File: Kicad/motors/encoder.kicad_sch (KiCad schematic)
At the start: 12 parts

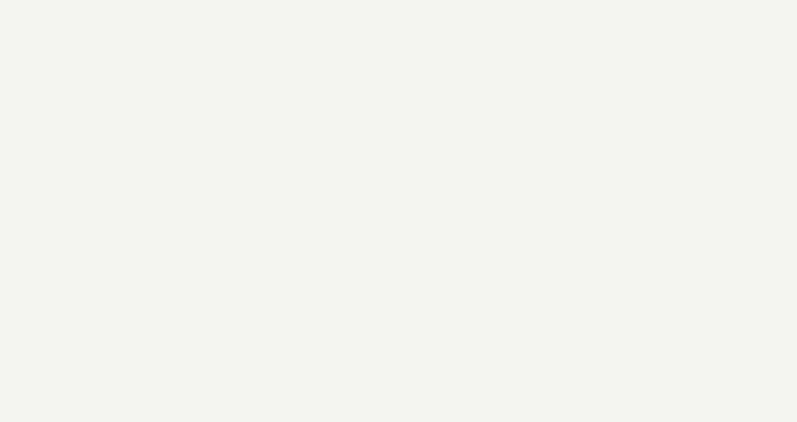
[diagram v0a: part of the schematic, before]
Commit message: Update Motors
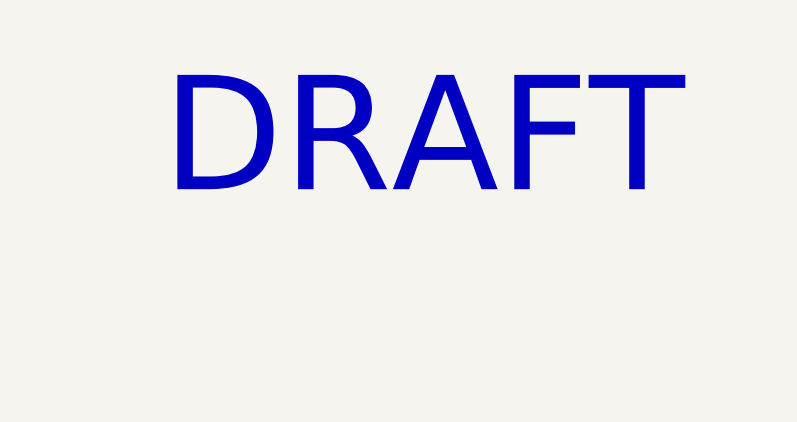
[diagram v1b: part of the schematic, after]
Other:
- note added: "DRAFT"
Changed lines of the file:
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@@
     (stroke (width 0) (type solid) (color 0 0 0 0))
+  )
+  (text "DRAFT" (at 127 93.98 0)
+    (effects (font (size 12.7 12.7)) (justify left bottom))
   )
   (symbol (lib_id "tronixio:SN74LVC1G19-SOT") (at 116.84 177.8 0) (unit 2)

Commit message: Update Motor
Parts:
- removed IC? (x4): SN74LVC1G19-SOT, tronixio:SOT-23-6, symbol tronixio:SN74LVC1G19-SOT
- removed TP?: KEYSTONE-5006, tronixio:KEYSTONE-5006, symbol tronixio:KEYSTONE-5006
- added C? (x2): 1µ, tronixio:CAPACITOR-1206, symbol tronixio:C-1206
- added R? (x2): 10K, tronixio:RESISTOR-1206, symbol tronixio:R-1206
- added TP?: HARWIN-S1751, tronixio:zzzHARWIN-S1751, symbol tronixio:HARWIN-S1751
- C? (x2): value C-1206 -> 100n; Name 100n -> (none)
- C? (x2): value C-1206 -> 1µ; Name 1µ -> (none)
- IC?: value LM3480-33-SOT -> LM3480-33; Name LM3480-33 -> (none)
- LED?: value LED-1206-ORANGE -> +3V3; symbol tronixio:LED-1206-ORANGE -> tronixio:LED-1206-RED; MOUSER 604-APT3216LSECKJ4RV -> 604-APT3216LSECKJ3RV
- R?: value R-1206 -> 6K8; Name 6K8 -> (none)
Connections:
- net +5V is gone; now on net +3V3: C?.1, C?.1, R?.1
- net +3V3: now also C?.1, C?.1, R?.1, R?.1, TP?.1
- net GND: now also C?.2, C?.2

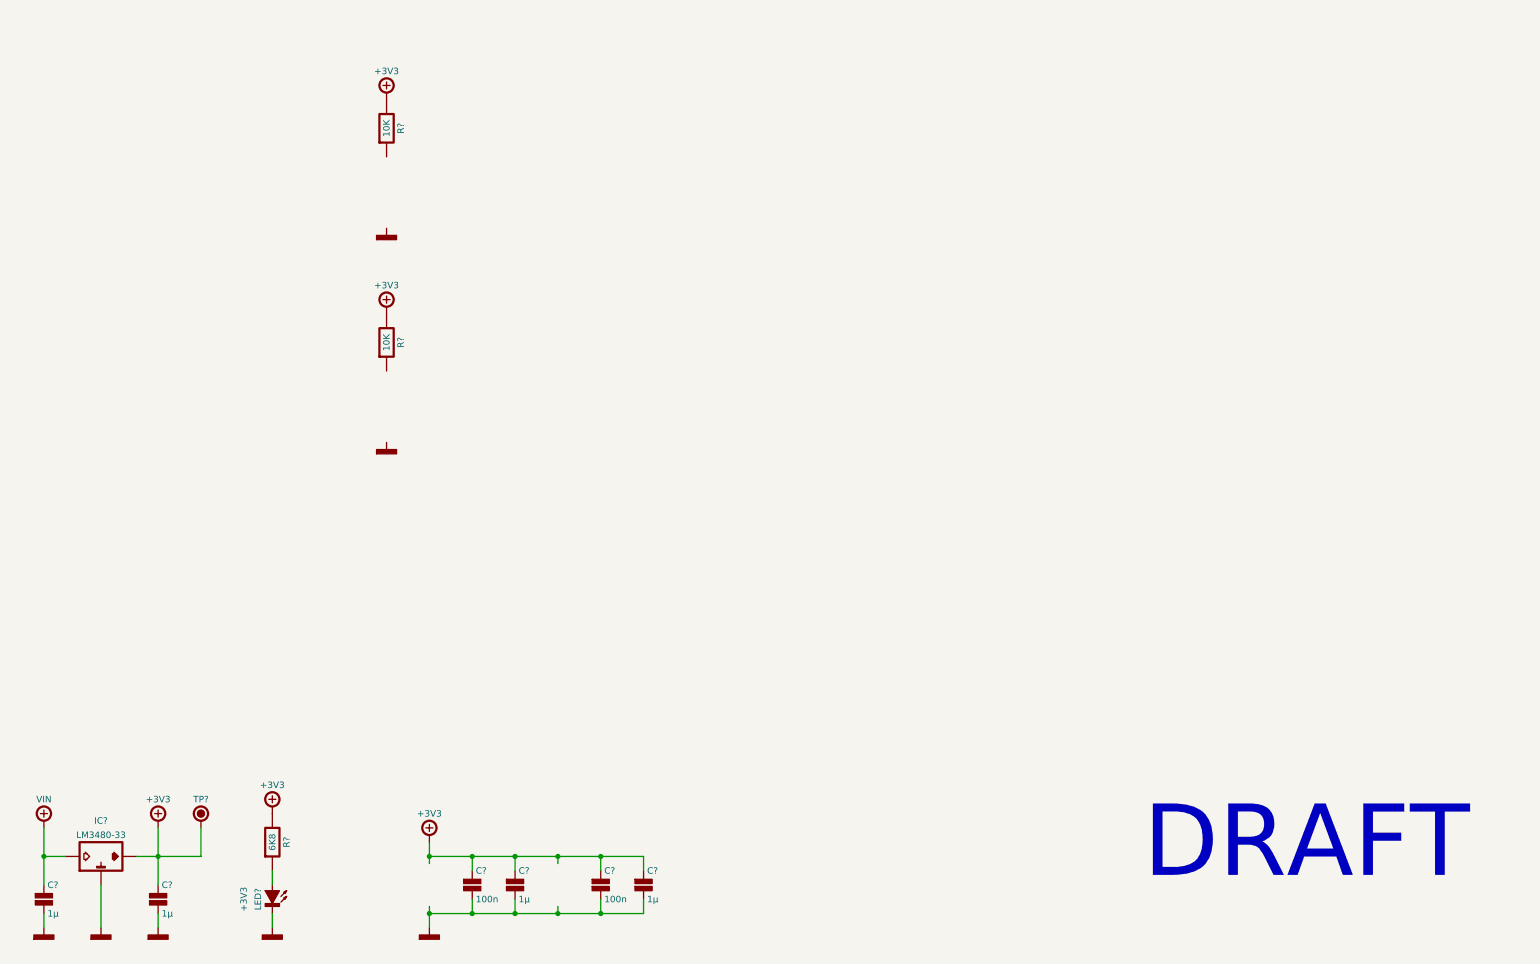
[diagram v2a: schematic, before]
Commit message: Update Motors
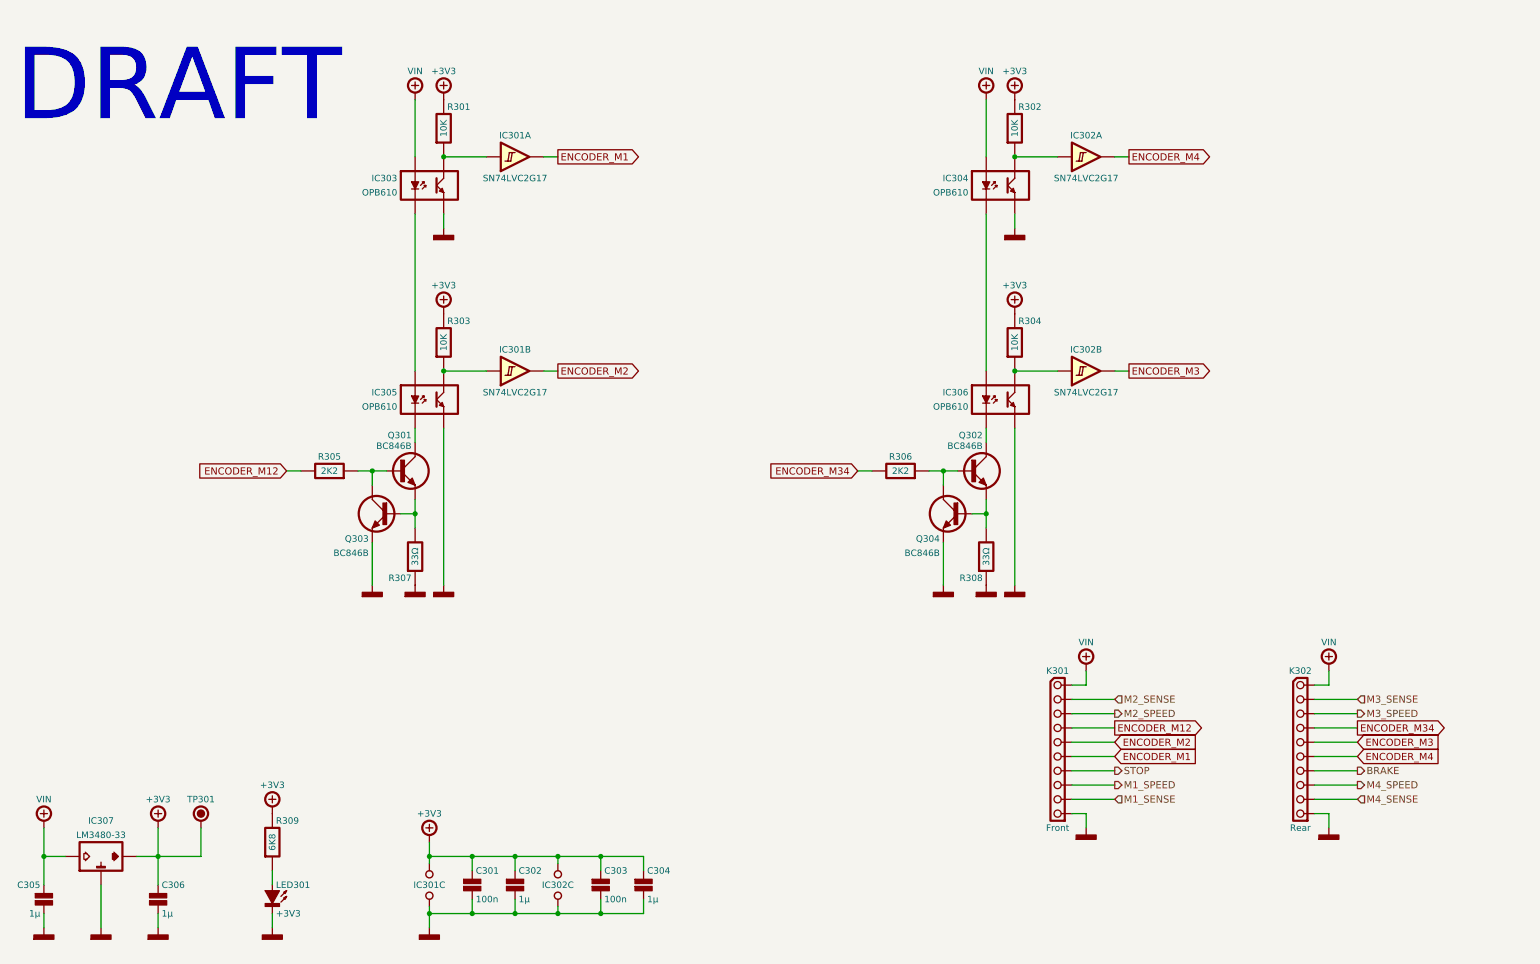
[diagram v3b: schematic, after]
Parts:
- removed R?: 10K, tronixio:RESISTOR-1206, symbol tronixio:R-1206
- added IC301, IC302: SN74LVC2G17, tronixio:SOT-23-6, symbol tronixio:SN74LVC2G17-SOT
- added IC303, IC304, IC305, IC306: OPB610, symbol tronixio:VISHAY-OPB610
- added K301: Front, tronixio:zzHARWIN-M20-782104x, symbol tronixio:HARWIN-254-F-1X10-VERTICAL
- added K302: Rear, tronixio:zzHARWIN-M20-782104x, symbol tronixio:HARWIN-254-F-1X10-VERTICAL
- added Q301, Q302, Q303, Q304: BC846B, tronixio:SOT-23-3, symbol tronixio:BC846BLT1G-SOT-23
- added R301, R302, R304: 10K, tronixio:RESISTOR-1206, symbol tronixio:R-1206
- added R305, R306: 2K2, tronixio:RESISTOR-1206, symbol tronixio:R-1206
- added R307, R308: 33Ω, tronixio:RESISTOR-1206, symbol tronixio:R-1206
- gave numbers to parts that had none: 11
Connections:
- net +3V3: now also IC301.6 (VCC), IC302.6 (VCC), R301.1, R302.1, R304.1
- net GND: now also IC301.2 (GND), IC302.2 (GND), IC303.4 (TRE), IC304.4 (TRE), IC305.4 (TRE), IC306.4 (TRE), K301.10 (Pin_10), K302.10 (Pin_10), Q303.2 (E), Q304.2 (E), R307.2, R308.2
- net VIN: now also IC303.2 (LEDA), IC304.2 (LEDA), K301.1 (Pin_1), K302.1 (Pin_1)
- net at R303.2: now also IC301.3 (2A), IC305.3 (TRC)
- new net: Q302.2 (E), Q304.1 (B), R308.1
- new net: Q302.1 (B), Q304.3 (C), R306.2
- new net: Q301.2 (E), Q303.1 (B), R307.1
- new net: Q301.1 (B), Q303.3 (C), R305.2
- new net: IC305.1 (LEDC), Q301.3 (C)
- new net: IC306.1 (LEDC), Q302.3 (C)
- new net: IC301.1 (1A), IC303.3 (TRC), R301.2
- new net: IC302.1 (1A), IC304.3 (TRC), R302.2
- new net: IC302.3 (2A), IC306.3 (TRC), R304.2
- new net: IC304.1 (LEDC), IC306.2 (LEDA)
- new net: IC303.1 (LEDC), IC305.2 (LEDA)
- new net BRAKE: K302.7 (Pin_7)
- new net ENCODER_M1: IC301.6 (1Y), K301.6 (Pin_6)
- new net ENCODER_M12: K301.4 (Pin_4), R305.1
- new net ENCODER_M2: IC301.4 (2Y), K301.5 (Pin_5)
- new net ENCODER_M3: IC302.4 (2Y), K302.5 (Pin_5)
- new net ENCODER_M34: K302.4 (Pin_4), R306.1
- new net ENCODER_M4: IC302.6 (1Y), K302.6 (Pin_6)
- new net M1_SENSE: K301.9 (Pin_9)
- new net M1_SPEED: K301.8 (Pin_8)
- new net M2_SENSE: K301.2 (Pin_2)
- new net M2_SPEED: K301.3 (Pin_3)
- new net M3_SENSE: K302.2 (Pin_2)
- new net M3_SPEED: K302.3 (Pin_3)
- new net M4_SENSE: K302.9 (Pin_9)
- new net M4_SPEED: K302.8 (Pin_8)
- new net STOP: K301.7 (Pin_7)
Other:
- moved on the sheet: R303

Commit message: Update Motor
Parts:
- IC303, IC304, IC305, IC306: footprint (none) -> tronixio:zzzOPB-610; symbol tronixio:VISHAY-OPB610 -> tronixio:TTE-OPB610
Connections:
- net +3V3: now also IC301.5 (VCC), IC302.5 (VCC); no longer IC301.6 (VCC), IC302.6 (VCC)
- net VIN: now also IC303.1 (LEDA), IC304.1 (LEDA); no longer IC303.2 (LEDA), IC304.2 (LEDA)
- net at Q301.3 (C): now also IC305.2 (LEDC); no longer IC305.1 (LEDC)
- net at Q302.3 (C): now also IC306.2 (LEDC); no longer IC306.1 (LEDC)
- new net: IC304.2 (LEDC), IC306.1 (LEDA)
- new net: IC303.2 (LEDC), IC305.1 (LEDA)
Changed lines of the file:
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@@
     (stroke (width 0) (type solid) (color 0 0 0 0))
   )
-  (text "DRAFT" (at 20.32 43.18 0)
-    (effects (font (size 12.7 12.7)) (justify left bottom))
+  (text "DRAFT" (at 208.28 187.96 0)
+    (effects (font (size 4 4)) (justify left bottom))
   )
   (global_label "ENCODER_M2" (shape output) (at 116.84 86.36 0) (fields_autoplaced)
@@
     (pin "1")
   )
-  (symbol (lib_name "SN74LVC2G17-SOT_3") (lib_id "tronixio:SN74LVC2G17-SOT") (at 210.82 86.36 0) (unit 2)
+  (symbol (lib_id "tronixio:SN74LVC2G17-SOT") (at 210.82 86.36 0) (unit 2)
     (in_bom yes) (on_board yes)
     (property "Reference" "IC302" (id 0) (at 210.82 82.55 0)
@@
     (pin "4")
   )
-  (symbol (lib_name "SN74LVC2G17-SOT_2") (lib_id "tronixio:SN74LVC2G17-SOT") (at 109.22 48.26 0) (unit 1)
+  (symbol (lib_id "tronixio:SN74LVC2G17-SOT") (at 109.22 48.26 0) (unit 1)
     (in_bom yes) (on_board yes)
     (property "Reference" "IC301" (id 0) (at 109.22 44.45 0)
@@
     (pin "1")
   )
-  (symbol (lib_id "tronixio:VISHAY-OPB610") (at 195.58 91.44 0) (unit 1)
+  (symbol (lib_id "tronixio:TTE-OPB610") (at 195.58 91.44 0) (unit 1)
     (in_bom yes) (on_board yes)
     (property "Reference" "IC306" (id 0) (at 189.865 90.17 0)
@@
       (effects (font (size 1.15 1.15)) (justify right))
     )
-    (property "Footprint" "" (id 2) (at 195.58 104.14 0)
+    (property "Footprint" "tronixio:zzzOPB-610" (id 2) (at 195.58 104.14 0)
       (effects (font (size 1 1)) hide)
     )
@@
     (pin "1")
   )
-  (symbol (lib_id "tronixio:VISHAY-OPB610") (at 93.98 53.34 0) (unit 1)
+  (symbol (lib_id "tronixio:TTE-OPB610") (at 93.98 53.34 0) (unit 1)
     (in_bom yes) (on_board yes)
     (property "Reference" "IC303" (id 0) (at 88.265 52.07 0)
@@
       (effects (font (size 1.15 1.15)) (justify right))
     )
-    (property "Footprint" "" (id 2) (at 93.98 66.04 0)
+    (property "Footprint" "tronixio:zzzOPB-610" (id 2) (at 93.98 66.04 0)
       (effects (font (size 1 1)) hide)
     )
@@
     (pin "9")
   )
-  (symbol (lib_name "SN74LVC2G17-SOT_1") (lib_id "tronixio:SN74LVC2G17-SOT") (at 109.22 86.36 0) (unit 2)
+  (symbol (lib_id "tronixio:SN74LVC2G17-SOT") (at 109.22 86.36 0) (unit 2)
     (in_bom yes) (on_board yes)
     (property "Reference" "IC301" (id 0) (at 109.22 82.55 0)
@@
     (pin "2")
   )
-  (symbol (lib_name "SN74LVC2G17-SOT_4") (lib_id "tronixio:SN74LVC2G17-SOT") (at 116.84 177.8 0) (unit 3)
+  (symbol (lib_id "tronixio:SN74LVC2G17-SOT") (at 116.84 177.8 0) (unit 3)
     (in_bom yes) (on_board yes)
     (property "Reference" "IC302" (id 0) (at 116.84 177.8 0)
@@
     )
     (pin "2")
-    (pin "6")
+    (pin "5")
   )
   (symbol (lib_id "tronixio:POWER-GND") (at 91.44 124.46 0) (unit 1)
@@
     )
     (pin "2")
+    (pin "5")
+  )
+  (symbol (lib_id "tronixio:POWER-+3V3") (at 198.12 76.2 0) (unit 1)
+    (in_bom yes) (on_board yes)
+    (property "Reference" "#PWR0308" (id 0) (at 198.12 88.9 0)
+      (effects (font (size 1 1)) hide)
+    )
+    (property "Value" "POWER-+3V3" (id 1) (at 198.12 86.36 0)
+      (effects (font (size 1 1)) hide)
+    )
+    (property "Footprint" "" (id 2) (at 198.12 76.2 0)
+      (effects (font (size 1 1)) hide)
+    )
+    (property "Datasheet" "" (id 3) (at 198.12 76.2 0)
+      (effects (font (size 1 1)) hide)
+    )
+    (property "Name" "+3V3" (id 4) (at 198.12 71.12 0)
+      (effects (font (size 1.15 1.15)))
+    )
+    (pin "1")
+  )
+  (symbol (lib_id "tronixio:POWER-VIN") (at 210.82 139.7 0) (unit 1)
+    (in_bom yes) (on_board yes)
+    (property "Reference" "#PWR0315" (id 0) (at 210.82 149.86 0)
+      (effects (font (size 1 1)) hide)
+    )
+    (property "Value" "POWER-VIN" (id 1) (at 210.82 152.4 0)
+      (effects (font (size 1 1)) hide)
+    )
+    (property "Footprint" "" (id 2) (at 210.82 139.7 0)
+      (effects (font (size 1 1)) hide)
+    )
+    (property "Datasheet" "" (id 3) (at 210.82 139.7 0)
+      (effects (font (size 1 1)) hide)
+    )
+    (property "Name" "VIN" (id 4) (at 210.82 134.62 0)
+      (effects (font (size 1.15 1.15)))
+    )
+    (pin "1")
+  )
+  (symbol (lib_id "tronixio:SN74LVC2G17-SOT") (at 210.82 48.26 0) (unit 1)
+    (in_bom yes) (on_board yes)
+    (property "Reference" "IC302" (id 0) (at 210.82 44.45 0)
+      (effects (font (size 1.15 1.15)))
+    )
+    (property "Value" "SN74LVC2G17" (id 1) (at 210.82 52.07 0)
+      (effects (font (size 1.15 1.15)))
+    )
+    (property "Footprint" "tronixio:SOT-23-6" (id 2) (at 210.82 53.34 0)
+      (effects (font (size 1 1)) hide)
+    )
+    (property "Datasheet" "http://www.ti.com/product/SN74LVC2G17" (id 3) (at 210.82 55.88 0)
+      (effects (font (size 1 1)) hide)
+    )
+    (property "MOUSER" "595-SN74LVC2G17DBVR" (id 4) (at 210.82 58.42 0)
+      (effects (font (size 1 1)) hide)
+    )
+    (pin "1")
     (pin "6")
   )
-  (symbol (lib_id "tronixio:POWER-+3V3") (at 198.12 76.2 0) (unit 1)
-    (in_bom yes) (on_board yes)
-    (property "Reference" "#PWR0308" (id 0) (at 198.12 88.9 0)
-      (effects (font (size 1 1)) hide)
-    )
-    (property "Value" "POWER-+3V3" (id 1) (at 198.12 86.36 0)
-      (effects (font (size 1 1)) hide)
-    )
-    (property "Footprint" "" (id 2) (at 198.12 76.2 0)
-      (effects (font (size 1 1)) hide)
-    )
-    (property "Datasheet" "" (id 3) (at 198.12 76.2 0)
-      (effects (font (size 1 1)) hide)
-    )
-    (property "Name" "+3V3" (id 4) (at 198.12 71.12 0)
-      (effects (font (size 1.15 1.15)))
-    )
-    (pin "1")
-  )
-  (symbol (lib_id "tronixio:POWER-VIN") (at 210.82 139.7 0) (unit 1)
-    (in_bom yes) (on_board yes)
-    (property "Reference" "#PWR0315" (id 0) (at 210.82 149.86 0)
-      (effects (font (size 1 1)) hide)
-    )
-    (property "Value" "POWER-VIN" (id 1) (at 210.82 152.4 0)
-      (effects (font (size 1 1)) hide)
-    )
-    (property "Footprint" "" (id 2) (at 210.82 139.7 0)
-      (effects (font (size 1 1)) hide)
-    )
-    (property "Datasheet" "" (id 3) (at 210.82 139.7 0)
-      (effects (font (size 1 1)) hide)
-    )
-    (property "Name" "VIN" (id 4) (at 210.82 134.62 0)
-      (effects (font (size 1.15 1.15)))
-    )
-    (pin "1")
-  )
-  (symbol (lib_name "SN74LVC2G17-SOT_3") (lib_id "tronixio:SN74LVC2G17-SOT") (at 210.82 48.26 0) (unit 1)
-    (in_bom yes) (on_board yes)
-    (property "Reference" "IC302" (id 0) (at 210.82 44.45 0)
-      (effects (font (size 1.15 1.15)))
-    )
-    (property "Value" "SN74LVC2G17" (id 1) (at 210.82 52.07 0)
-      (effects (font (size 1.15 1.15)))
-    )
-    (property "Footprint" "tronixio:SOT-23-6" (id 2) (at 210.82 53.34 0)
-      (effects (font (size 1 1)) hide)
-    )
-    (property "Datasheet" "http://www.ti.com/product/SN74LVC2G17" (id 3) (at 210.82 55.88 0)
-      (effects (font (size 1 1)) hide)
-    )
-    (property "MOUSER" "595-SN74LVC2G17DBVR" (id 4) (at 210.82 58.42 0)
-      (effects (font (size 1 1)) hide)
-    )
-    (pin "1")
-    (pin "6")
-  )
   (symbol (lib_id "tronixio:POWER-+3V3") (at 96.52 38.1 0) (unit 1)
     (in_bom yes) (on_board yes)
@@
     (pin "1")
   )
-  (symbol (lib_id "tronixio:VISHAY-OPB610") (at 93.98 91.44 0) (unit 1)
+  (symbol (lib_id "tronixio:TTE-OPB610") (at 93.98 91.44 0) (unit 1)
     (in_bom yes) (on_board yes)
     (property "Reference" "IC305" (id 0) (at 88.265 90.17 0)
@@
       (effects (font (size 1.15 1.15)) (justify right))
     )
-    (property "Footprint" "" (id 2) (at 93.98 104.14 0)
+    (property "Footprint" "tronixio:zzzOPB-610" (id 2) (at 93.98 104.14 0)
       (effects (font (size 1 1)) hide)
     )
@@
     (pin "3")
   )
-  (symbol (lib_id "tronixio:VISHAY-OPB610") (at 195.58 53.34 0) (unit 1)
+  (symbol (lib_id "tronixio:TTE-OPB610") (at 195.58 53.34 0) (unit 1)
     (in_bom yes) (on_board yes)
     (property "Reference" "IC304" (id 0) (at 189.865 52.07 0)
@@
       (effects (font (size 1.15 1.15)) (justify right))
     )
-    (property "Footprint" "" (id 2) (at 195.58 66.04 0)
-      (effects (font (size 1 1)) hide)
-    )
+    (property "Footprint" "tronixio:zzzOPB-610" (id 2) (at 195.58 66.04 0)
+      (effects (font (size 1 1)) hide)
+    )

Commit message: Update
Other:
- title: Motor Encoder -> Motors Encoder
- moved on the sheet: R309
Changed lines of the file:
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@@
   (paper "A4")
   (title_block
-    (title "Motor Encoder")
+    (title "Motors Encoder")
     (date "01/2022")
     (rev "A")
@@
   (wire (pts (xy 185.42 104.14) (xy 187.96 104.14))
     (stroke (width 0) (type default) (color 0 0 0 0))
-  )
-  (wire (pts (xy 66.04 175.26) (xy 66.04 177.8))
-    (stroke (width 0) (type solid) (color 0 0 0 0))
   )
   (wire (pts (xy 215.9 144.78) (xy 208.28 144.78))
@@
     (pin "2")
   )
-  (symbol (lib_id "tronixio:POWER-+3V3") (at 66.04 165.1 0) (unit 1)
-    (in_bom yes) (on_board yes)
-    (property "Reference" "#PWR0317" (id 0) (at 66.04 177.8 0)
-      (effects (font (size 1 1)) hide)
-    )
-    (property "Value" "POWER-+3V3" (id 1) (at 66.04 175.26 0)
-      (effects (font (size 1 1)) hide)
-    )
-    (property "Footprint" "" (id 2) (at 66.04 165.1 0)
-      (effects (font (size 1 1)) hide)
-    )
-    (property "Datasheet" "" (id 3) (at 66.04 165.1 0)
-      (effects (font (size 1 1)) hide)
-    )
-    (property "Name" "+3V3" (id 4) (at 66.04 160.02 0)
+  (symbol (lib_id "tronixio:POWER-+3V3") (at 66.04 167.64 0) (unit 1)
+    (in_bom yes) (on_board yes)
+    (property "Reference" "#PWR0317" (id 0) (at 66.04 180.34 0)
+      (effects (font (size 1 1)) hide)
+    )
+    (property "Value" "POWER-+3V3" (id 1) (at 66.04 177.8 0)
+      (effects (font (size 1 1)) hide)
+    )
+    (property "Footprint" "" (id 2) (at 66.04 167.64 0)
+      (effects (font (size 1 1)) hide)
+    )
+    (property "Datasheet" "" (id 3) (at 66.04 167.64 0)
+      (effects (font (size 1 1)) hide)
+    )
+    (property "Name" "+3V3" (id 4) (at 66.04 162.56 0)
       (effects (font (size 1.15 1.15)))
     )
@@
     (pin "1")
   )
-  (symbol (lib_id "tronixio:R-1206") (at 66.04 170.18 0) (unit 1)
-    (in_bom yes) (on_board yes)
-    (property "Reference" "R309" (id 0) (at 66.675 166.37 0)
-      (effects (font (size 1.15 1.15)) (justify left))
-    )
-    (property "Value" "6K8" (id 1) (at 66.04 170.18 90)
-      (effects (font (size 1.15 1.15)))
-    )
-    (property "Footprint" "tronixio:RESISTOR-1206" (id 2) (at 66.04 182.88 0)
-      (effects (font (size 1 1)) hide)
-    )
-    (property "Datasheet" "" (id 3) (at 66.04 170.18 0)
-      (effects (font (size 1 1)) hide)
-    )
+  (symbol (lib_id "tronixio:R-1206") (at 66.04 172.72 0) (unit 1)
+    (in_bom yes) (on_board yes)
+    (property "Reference" "R309" (id 0) (at 66.675 168.91 0)
+      (effects (font (size 1.15 1.15)) (justify left))
+    )
+    (property "Value" "6K8" (id 1) (at 66.04 172.72 90)
+      (effects (font (size 1.15 1.15)))
+    )
+    (property "Footprint" "tronixio:RESISTOR-1206" (id 2) (at 66.04 185.42 0)
+      (effects (font (size 1 1)) hide)
+    )
+    (property "Datasheet" "" (id 3) (at 66.04 172.72 0)
+      (effects (font (size 1 1)) hide)
+    )
